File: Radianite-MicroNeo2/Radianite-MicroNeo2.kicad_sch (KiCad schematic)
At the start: 81 parts, among them J1 Micro_SD_Card_Det1, J2 USB_C_Receptacle_USB2.0_16P, J3 USB_C_Receptacle_USB2.0_16P, J4 AudioJack4, J6 Conn_02x16_Odd_Even, SW1 SW_Push, SW2 SW_SPDT, U1 F1C200s, U3 CH340E, U4 W25Q32JVZP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

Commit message: fixes to the microneo 2
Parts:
- AE1: footprint RF_Antenna:Johanson_2450AT18x100 -> Connector_Coaxial:U.FL_Molex_MCRF_73412-0110_Vertical
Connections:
- net GND: now also AE1.2 (PCB_Trace)
- no-connect marks 48 -> 47
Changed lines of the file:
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@@
 	)
 	(no_connect
-		(at 397.51 177.8)
-	)
-	(no_connect
 		(at 71.12 247.65)
 	)
@@
 	(wire
 		(pts
+			(xy 397.51 177.8) (xy 397.51 189.23)
+		)
+		(stroke
+			(width 0)
+			(type default)
+		)
+	)
+	(wire
+		(pts
 			(xy 137.16 256.54) (xy 154.94 256.54)
 		)
@@
 			)
 		)
-		(property "Footprint" "RF_Antenna:Johanson_2450AT18x100"
+		(property "Footprint" "Connector_Coaxial:U.FL_Molex_MCRF_73412-0110_Vertical"
 			(at 392.43 170.815 0)
 			(effects
@@
 					(unit 1)
 				)
+			)
+		)
+	)
+	(symbol
+		(lib_id "power:GND")
+		(at 397.51 189.23 0)
+		(unit 1)
+		(exclude_from_sim no)
+		(in_bom yes)
+		(on_board yes)
+		(dnp no)
+		(fields_autoplaced yes)
+		(property "Reference" "#PWR046"
+			(at 397.51 195.58 0)
+			(effects
+				(font
+					(size 1.27 1.27)
+				)
+				(hide yes)
+			)
+		)
+		(property "Value" "GND"
+			(at 397.51 194.31 0)
+			(effects
+				(font
+					(size 1.27 1.27)
+				)
+			)
+		)
+		(property "Footprint" ""
+			(at 397.51 189.23 0)
+			(effects
+				(font
+					(size 1.27 1.27)
+				)
+				(hide yes)
+			)
+		)
+		(property "Datasheet" ""
+			(at 397.51 189.23 0)
+			(effects
+				(font
+					(size 1.27 1.27)
+				)
+				(hide yes)
+			)
+		)
+		(property "Description" "Power symbol creates a global label with name \"GND\" , ground"
+			(at 397.51 189.23 0)
+			(effects
+				(font
+					(size 1.27 1.27)
+				)
+				(hide yes)
+			)
+		)
+		(pin "1"
+		)
+		(instances
+			(project "Radianite-MicroNeo2"
+				(path "/802e0cb3-e09e-42e9-bc92-71c64f8b919b"
+					(reference "#PWR046")
+					(unit 1)
+				)

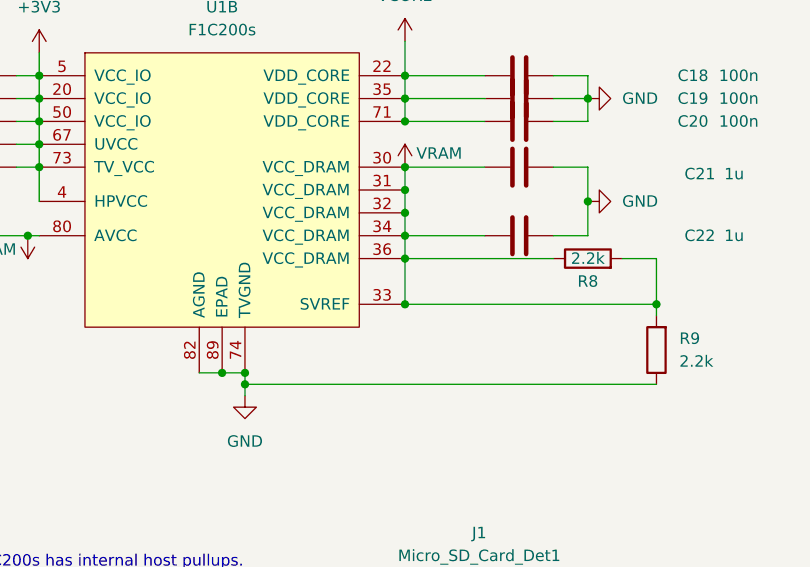
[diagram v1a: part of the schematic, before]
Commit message: turns out SVREF is a divided voltage between DRAM
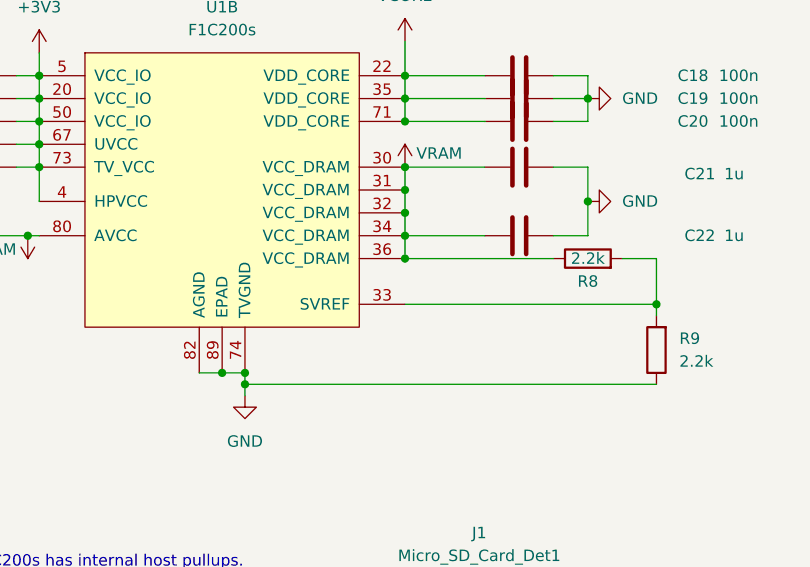
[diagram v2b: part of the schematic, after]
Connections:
- net VRAM: no longer R8.2, R9.2, U1.33 (SVREF)
- new net: R8.2, R9.2, U1.33 (SVREF)
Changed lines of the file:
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@@
-	)
-	(junction
-		(at 345.44 74.93)
-		(diameter 0)
-		(color 0 0 0 0)
 	)
 	(junction
@@
 		)
 		(stroke
-			(width 0)
-			(type default)
-		)
-	)
-	(wire
-		(pts
-			(xy 345.44 69.85) (xy 345.44 74.93)
-		)
-		(stroke

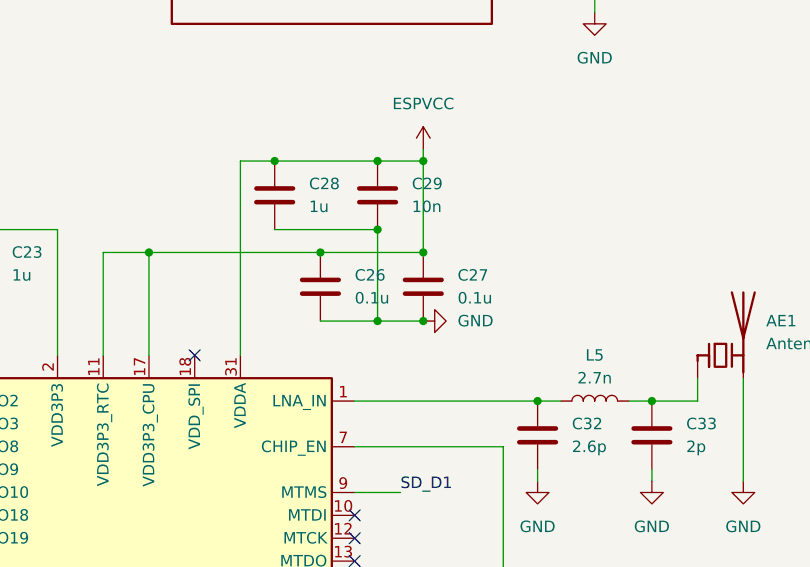
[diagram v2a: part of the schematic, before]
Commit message: woopsies, wrong sd card direction
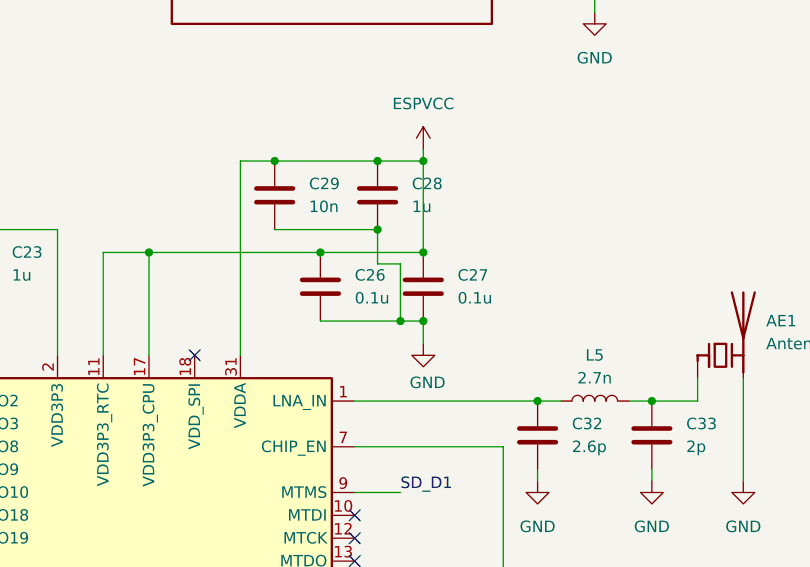
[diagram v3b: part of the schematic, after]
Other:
- moved on the sheet: C28, C29
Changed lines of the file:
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@@
 	)
 	(junction
+		(at 356.87 153.67)
+		(diameter 0)
+		(color 0 0 0 0)
+	)
+	(junction
 		(at 212.09 238.76)
 		(diameter 0)
@@
 	)
 	(junction
-		(at 345.44 153.67)
-		(diameter 0)
-		(color 0 0 0 0)
-	)
-	(junction
 		(at 121.92 264.16)
 		(diameter 0)
@@
 	)
 	(junction
-		(at 356.87 153.67)
+		(at 304.8 54.61)
 		(diameter 0)
 		(color 0 0 0 0)
 	)
 	(junction
-		(at 304.8 54.61)
+		(at 356.87 161.29)
 		(diameter 0)
 		(color 0 0 0 0)
@@
 	)
 	(junction
-		(at 356.87 161.29)
-		(diameter 0)
-		(color 0 0 0 0)
-	)
-	(junction
 		(at 345.44 49.53)
 		(diameter 0)
@@
 	)
 	(junction
-		(at 356.87 171.45)
-		(diameter 0)
-		(color 0 0 0 0)
-	)
-	(junction
 		(at 361.95 163.83)
 		(diameter 0)
@@
 	)
 	(junction
+		(at 345.44 153.67)
+		(diameter 0)
+		(color 0 0 0 0)
+	)
+	(junction
 		(at 270.51 101.6)
 		(diameter 0)
@@
 	)
 	(junction
+		(at 359.41 171.45)
+		(diameter 0)
+		(color 0 0 0 0)
+	)
+	(junction
 		(at 187.96 269.24)
 		(diameter 0)
@@
 	(wire
 		(pts
+			(xy 345.44 153.67) (xy 356.87 153.67)
+		)
+		(stroke
+			(width 0)
+			(type default)
+		)
+	)
+	(wire
+		(pts
 			(xy 365.76 63.5) (xy 365.76 67.31)
 		)
@@
 	(wire
 		(pts
+			(xy 361.95 173.99) (xy 361.95 171.45)
+		)
+		(stroke
+			(width 0)
+			(type default)
+		)
+	)
+	(wire
+		(pts
 			(xy 297.18 236.22) (xy 297.18 237.49)
 		)
@@
 	(wire
 		(pts
-			(xy 345.44 153.67) (xy 356.87 153.67)
-		)
-		(stroke
-			(width 0)
-			(type default)
-		)
-	)
-	(wire
-		(pts
 			(xy 64.77 67.31) (xy 67.31 67.31)
 		)
@@
 	(wire
 		(pts
+			(xy 356.87 161.29) (xy 356.87 165.1)
+		)
+		(stroke
+			(width 0)
+			(type default)
+		)
+	)
+	(wire
+		(pts
 			(xy 299.72 168.91) (xy 312.42 168.91)
 		)
@@
 	(wire
 		(pts
+			(xy 345.44 161.29) (xy 356.87 161.29)
+		)
+		(stroke
+			(width 0)
+			(type default)
+		)
+	)
+	(wire
+		(pts
 			(xy 187.96 269.24) (xy 190.5 269.24)
 		)
@@
 	(wire
 		(pts
-			(xy 356.87 153.67) (xy 361.95 153.67)
-		)
-		(stroke
-			(width 0)
-			(type default)
-		)
-	)
-	(wire
-		(pts
 			(xy 113.03 256.54) (xy 121.92 256.54)
 		)
@@
 	(wire
 		(pts
-			(xy 350.52 171.45) (xy 356.87 171.45)
+			(xy 113.03 233.68) (xy 121.92 233.68)
 		)
 		(stroke
@@
 	(wire
 		(pts
-			(xy 113.03 233.68) (xy 121.92 233.68)
+			(xy 208.28 257.81) (xy 212.09 257.81)
 		)
 		(stroke
@@
 	(wire
 		(pts
-			(xy 208.28 257.81) (xy 212.09 257.81)
+			(xy 243.84 105.41) (xy 247.65 105.41)
 		)
 		(stroke
@@
 	(wire
 		(pts
-			(xy 243.84 105.41) (xy 247.65 105.41)
+			(xy 228.6 241.3) (xy 238.76 241.3)
 		)
 		(stroke
@@
 	(wire
 		(pts
-			(xy 228.6 241.3) (xy 238.76 241.3)
+			(xy 304.8 52.07) (xy 304.8 54.61)
 		)
 		(stroke
@@
 	(wire
 		(pts
-			(xy 304.8 52.07) (xy 304.8 54.61)
+			(xy 118.11 241.3) (xy 118.11 252.73)
 		)
 		(stroke
@@
 	(wire
 		(pts
-			(xy 118.11 241.3) (xy 118.11 252.73)
+			(xy 356.87 165.1) (xy 359.41 165.1)
 		)
 		(stroke
@@
 	(wire
 		(pts
+			(xy 356.87 153.67) (xy 361.95 153.67)
+		)
+		(stroke
+			(width 0)
+			(type default)
+		)
+	)
+	(wire
+		(pts
 			(xy 120.65 120.65) (xy 134.62 120.65)
 		)
@@
 	(wire
 		(pts
-			(xy 345.44 161.29) (xy 356.87 161.29)
-		)
-		(stroke
-			(width 0)
-			(type default)
-		)
-	)
-	(wire
-		(pts
 			(xy 77.47 62.23) (xy 81.28 62.23)
 		)
@@
 	(wire
 		(pts
+			(xy 359.41 171.45) (xy 361.95 171.45)
+		)
+		(stroke
+			(width 0)
+			(type default)
+		)
+	)
+	(wire
+		(pts
 			(xy 205.74 67.31) (xy 208.28 67.31)
 		)
@@
 	(wire
 		(pts
-			(xy 356.87 171.45) (xy 361.95 171.45)
+			(xy 350.52 171.45) (xy 359.41 171.45)
 		)
 		(stroke
@@
 	(wire
 		(pts
+			(xy 359.41 165.1) (xy 359.41 171.45)
+		)
+		(stroke
+			(width 0)
+			(type default)
+		)
+	)
+	(wire
+		(pts
 			(xy 243.84 171.45) (xy 259.08 171.45)
 		)
@@
 	(wire
 		(pts
-			(xy 356.87 161.29) (xy 356.87 171.45)
-		)
-		(stroke
-			(width 0)
-			(type default)
-		)
-	)
-	(wire
-		(pts
 			(xy 302.26 59.69) (xy 304.8 59.69)
 		)
@@
 	(symbol
 		(lib_id "Device:C")
-		(at 356.87 157.48 0)
+		(at 345.44 157.48 0)
 		(unit 1)
 		(exclude_from_sim no)
@@
 		(fields_autoplaced yes)
 		(property "Reference" "C29"
-			(at 360.68 156.21 0)
+			(at 349.25 156.21 0)
 			(effects
 				(font
@@
 		)
 		(property "Value" "10n"
-			(at 360.68 158.75 0)
+			(at 349.25 158.75 0)
 			(effects
 				(font
@@
 		)
 		(property "Footprint" "Capacitor_SMD:C_0402_1005Metric"
-			(at 357.8352 161.29 0)
+			(at 346.4052 161.29 0)
 			(effects
 				(font
@@
 		)
 		(property "Datasheet" "~"
-			(at 356.87 157.48 0)
+			(at 345.44 157.48 0)
 			(effects
 				(font
@@
 		)
 		(property "Description" "Unpolarized capacitor"
-			(at 356.87 157.48 0)
+			(at 345.44 157.48 0)
 			(effects
 				(font
@@
 	(symbol
 		(lib_id "power:GND")
-		(at 361.95 171.45 90)
+		(at 361.95 173.99 0)
 		(unit 1)
 		(exclude_from_sim no)
@@
 		(on_board yes)
 		(dnp no)
-		(fields_autoplaced yes)
 		(property "Reference" "#PWR043"
-			(at 368.3 171.45 0)
+			(at 361.95 180.34 0)
 			(effects
 				(font
@@
 		)
 		(property "Value" "GND"
-			(at 365.76 171.45 90)
+			(at 360.426 178.308 0)
 			(effects
 				(font
 					(size 1.27 1.27)
 				)
-				(justify right)
+				(justify left)
 			)
 		)
 		(property "Footprint" ""
-			(at 361.95 171.45 0)
+			(at 361.95 173.99 0)
 			(effects
 				(font
@@
 		)
 		(property "Datasheet" ""
-			(at 361.95 171.45 0)
+			(at 361.95 173.99 0)
 			(effects
 				(font
@@
 		)
 		(property "Description" "Power symbol creates a global label with name \"GND\" , ground"
-			(at 361.95 171.45 0)
+			(at 361.95 173.99 0)
 			(effects
 				(font
@@
 	(symbol
 		(lib_id "Device:C")
-		(at 345.44 157.48 0)
+		(at 356.87 157.48 0)
 		(unit 1)
 		(exclude_from_sim no)
@@
 		(fields_autoplaced yes)
 		(property "Reference" "C28"
-			(at 349.25 156.21 0)
+			(at 360.68 156.21 0)
 			(effects
 				(font
@@
 		)
 		(property "Value" "1u"
-			(at 349.25 158.75 0)
+			(at 360.68 158.75 0)
 			(effects
 				(font
@@
 		)
 		(property "Footprint" "Capacitor_SMD:C_0402_1005Metric"
-			(at 346.4052 161.29 0)
+			(at 357.8352 161.29 0)
 			(effects
 				(font
@@
 		)
 		(property "Datasheet" "~"
-			(at 345.44 157.48 0)
+			(at 356.87 157.48 0)
 			(effects
 				(font
@@
 		)
 		(property "Description" "Unpolarized capacitor"
-			(at 345.44 157.48 0)
+			(at 356.87 157.48 0)
 			(effects
 				(font

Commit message: 6/3/2025 upstream sync
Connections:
- net XTAL-: now reaches C31.1, U5.29 (XTAL_N), Y2.1
- net XTAL+: now reaches C30.1, U5.30 (XTAL_P), Y2.3
- net OTG_DM renamed OTG_D-
- net OTG_DP renamed OTG_D+
- net TTL_DM renamed TTL_D-
- net TTL_DP renamed TTL_D+
